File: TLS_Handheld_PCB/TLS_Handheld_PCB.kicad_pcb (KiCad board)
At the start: 4 copper layers, 175 x 100 mm, 89 parts, among them J1 Conn_01x02_Pin, J2 Conn_01x02_Pin, J3 Conn_01x02_Pin, M1 TO-236AB_SOT23_NEX, M2 TO-236AB_SOT23_NEX, U1 LT8640SEV_PBF, U2 LT8640SEV_PBF, U3 LT8619EDD-TRPBF, U4 LAA108STR, U5 SOP65P640X110-14N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

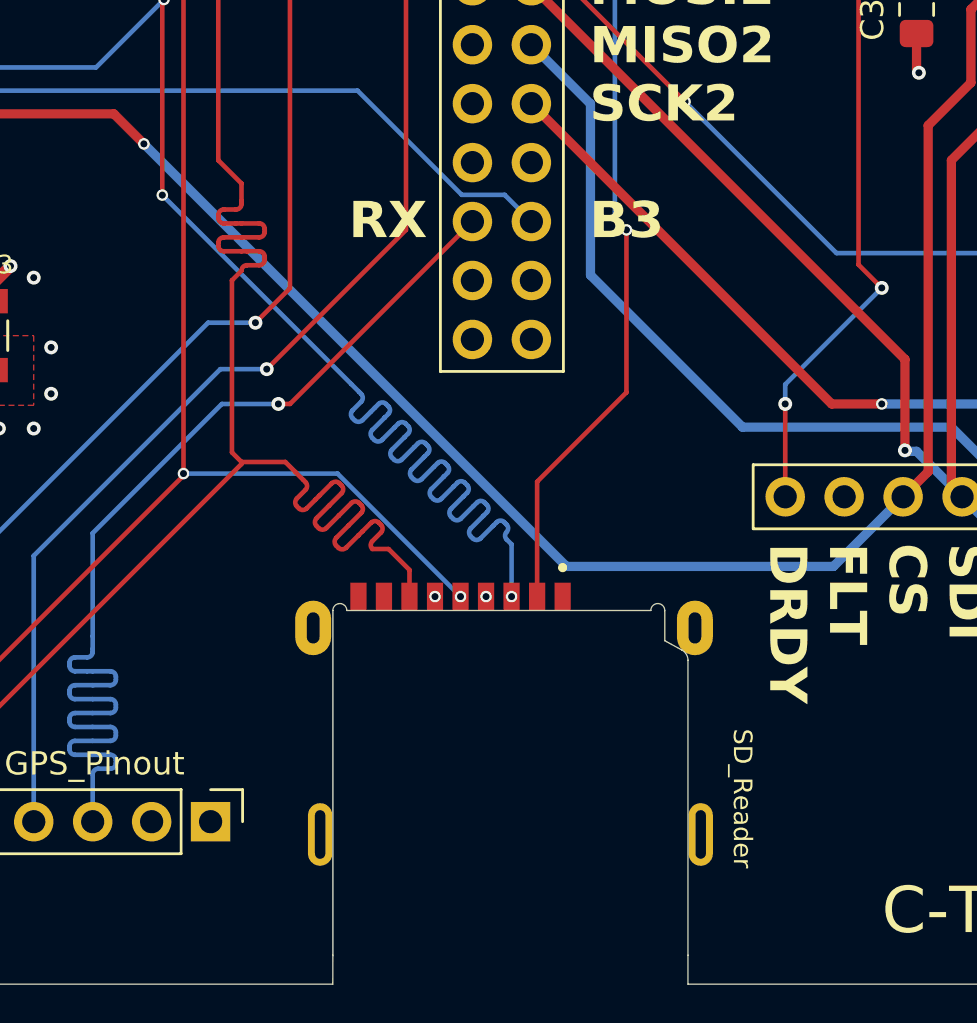
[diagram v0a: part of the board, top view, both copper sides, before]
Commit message: Fix Clearance issues with sd card
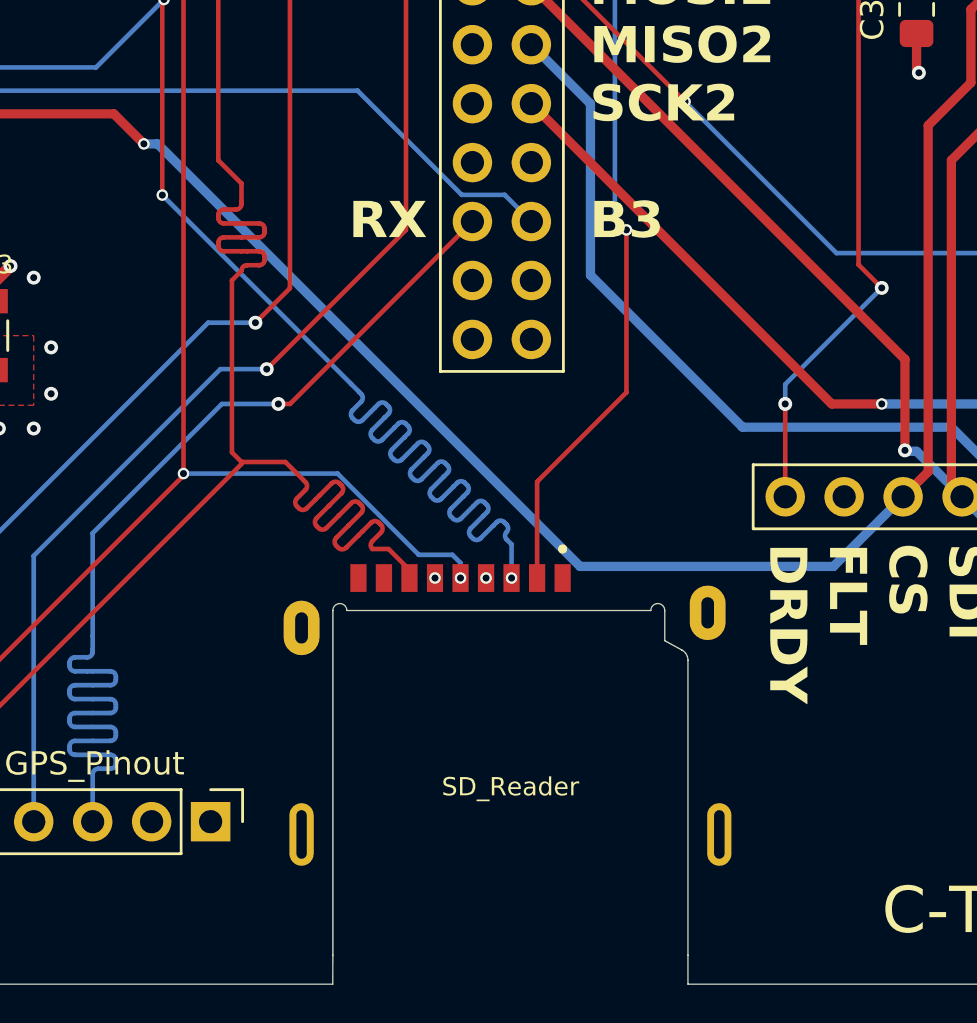
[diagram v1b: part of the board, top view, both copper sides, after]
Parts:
- SD_Reader: footprint My_PCB_Library:CUI_MSD-3-A -> Library:CUI_MSD-3-A
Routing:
- net TOUCH_MISO: track 181.4 -> 180.6 mm
- net DISPL_MOSI: track 211.3 -> 210.5 mm
- net SD_CS: track 60.1 -> 59.3 mm
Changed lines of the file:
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@@
 		(embedded_fonts no)
 	)
-	(footprint "My_PCB_Library:CUI_MSD-3-A"
+	(footprint "Library:CUI_MSD-3-A"
 		(layer "F.Cu")
 		(at 165.5 133.5)
 		(property "Reference" "SD_Reader"
-			(at 10 0.5 270)
-			(unlocked yes)
+			(at 0 0 0)
 			(layer "F.SilkS")
 			(effects
 				(font
-					(size 0.8 0.8)
+					(size 0.787402 0.787402)
 					(thickness 0.15)
 				)
@@
 		(attr smd)
 		(fp_circle
-			(center 2.25 -9.45)
-			(end 2.35 -9.45)
+			(center 2.25 -10.25)
+			(end 2.35 -10.25)
 			(stroke
 				(width 0.2)
@@
 		)
 		(fp_line
-			(start -9.525 -9.05)
-			(end 8.975 -9.05)
+			(start -10.5 -10)
+			(end 9.5 -10)
 			(stroke
 				(width 0.05)
@@
 		)
 		(fp_line
-			(start -9.525 13.1)
-			(end -9.525 -9.05)
+			(start -10.5 13.1)
+			(end -10.5 -10)
 			(stroke
 				(width 0.05)
@@
 		)
 		(fp_line
-			(start 8.975 -9.05)
-			(end 8.975 13.1)
+			(start 9.5 -10)
+			(end 9.5 13.1)
 			(stroke
 				(width 0.05)
@@
 		)
 		(fp_line
-			(start 8.975 13.1)
-			(end -9.525 13.1)
+			(start 9.5 13.1)
+			(end -10.5 13.1)
 			(stroke
 				(width 0.05)
@@
 		)
 		(pad "1" smd rect
-			(at 2.25 -8.2)
+			(at 2.25 -9)
 			(size 0.7 1.2)
 			(layers "F.Cu" "F.Mask" "F.Paste")
@@
 		)
 		(pad "2" smd rect
-			(at 1.15 -8.2)
+			(at 1.15 -9)
 			(size 0.7 1.2)
 			(layers "F.Cu" "F.Mask" "F.Paste")
@@
 		)
 		(pad "3" smd rect
-			(at 0.05 -8.2)
+			(at 0.05 -9)
 			(size 0.7 1.2)
 			(layers "F.Cu" "F.Mask" "F.Paste")
@@
 		)
 		(pad "4" smd rect
-			(at -1.05 -8.2)
+			(at -1.05 -9)
 			(size 0.7 1.2)
 			(layers "F.Cu" "F.Mask" "F.Paste")
@@
 		)
 		(pad "5" smd rect
-			(at -2.15 -8.2)
+			(at -2.15 -9)
 			(size 0.7 1.2)
 			(layers "F.Cu" "F.Mask" "F.Paste")
@@
 		)
 		(pad "6" smd rect
-			(at -3.25 -8.2)
+			(at -3.25 -9)
 			(size 0.7 1.2)
 			(layers "F.Cu" "F.Mask" "F.Paste")
@@
 		)
 		(pad "7" smd rect
-			(at -4.35 -8.2)
+			(at -4.35 -9)
 			(size 0.7 1.2)
 			(layers "F.Cu" "F.Mask" "F.Paste")
@@
 		)
 		(pad "8" smd rect
-			(at -5.45 -8.2)
+			(at -5.45 -9)
 			(size 0.7 1.2)
 			(layers "F.Cu" "F.Mask" "F.Paste")
@@
 		)
 		(pad "CD" smd rect
-			(at -6.55 -8.2)
+			(at -6.55 -9)
 			(size 0.7 1.2)
 			(layers "F.Cu" "F.Mask" "F.Paste")
@@
 		)
 		(pad "G1" thru_hole oval
-			(at -8.5 -6.85)
+			(at -9 -6.85)
 			(size 1.55 2.35)
 			(drill oval 0.55 1.35)
@@
 		)
 		(pad "G2" thru_hole oval
-			(at 7.95 -6.85)
+			(at 8.5 -7.5)
 			(size 1.55 2.35)
 			(drill oval 0.55 1.35)
@@
 		)
 		(pad "G3" thru_hole oval
-			(at -8.2 2.05)
+			(at -9 2.05)
 			(size 1.05 2.7)
 			(drill oval 0.45 2.1)
@@
 		)
 		(pad "G4" thru_hole oval
-			(at 8.2 2.05)
+			(at 9 2.05)
 			(size 1.05 2.7)
 			(drill oval 0.45 2.1)
@@
 		)
 		(embedded_fonts no)
-		(model "C:/Users/cbyer/Documents/_gitRepos/ENGG4000_PowerPCB/Components/SD_Card/MSD_3_A/MSD-3-A.step"
-			(offset
-				(xyz -7.5 -7 -0.85)
-			)
-			(scale
-				(xyz 1 1 1)
-			)
-			(rotate
-				(xyz 90 180 180)
-			)
-		)
 	)
 	(footprint "Capacitor_SMD:C_0805_2012Metric_Pad1.18x1.45mm_HandSolder"
@@
 	)
 	(via
-		(at 162.25 125.3)
+		(at 162.25 124.5)
 		(size 0.5)
 		(drill 0.3)
@@
 	)
 	(segment
-		(start 167.9125 124)
+		(start 168.5 124)
 		(end 179.42 124)
 		(width 0.4)
@@
 	(segment
 		(start 149.70625 105.79375)
-		(end 167.9125 124)
+		(end 150.29375 105.79375)
 		(width 0.4)
 		(layer "B.Cu")
@@
 	)
 	(segment
+		(start 150.29375 105.79375)
+		(end 168.5 124)
+		(width 0.4)
+		(layer "B.Cu")
+		(net 48)
+	)
+	(segment
 		(start 222.065 92.5)
 		(end 221 92.5)
@@
 	)
 	(via
-		(at 164.45 125.3)
+		(at 164.45 124.5)
 		(size 0.5)
 		(drill 0.3)
@@
 	)
 	(via
-		(at 165.55 125.3)
+		(at 165.55 124.5)
 		(size 0.5)
 		(drill 0.3)
@@
 	)
 	(segment
+		(start 165.55 123.05)
+		(end 165.334969 122.834969)
+		(width 0.2)
+		(layer "B.Cu")
+		(net 64)
+	)
+	(segment
 		(start 106.4125 117.5)
 		(end 116.9125 107)
@@
 	)
 	(segment
+		(start 165.55 124.5)
+		(end 165.55 123.05)
+		(width 0.2)
+		(layer "B.Cu")
+		(net 64)
+	)
+	(segment
 		(start 84 109.123531)
 		(end 84 109.243531)
@@
 	)
 	(segment
-		(start 165.55 125.3)
-		(end 165.55 123.05)
-		(width 0.2)
-		(layer "B.Cu")
-		(net 64)
-	)
-	(segment
 		(start 160.933205 118.433204)
 		(end 160.933204 118.433204)
@@
 	)
 	(segment
-		(start 165.55 123.05)
-		(end 165.334969 122.834969)
-		(width 0.2)
-		(layer "B.Cu")
-		(net 64)
-	)
-	(segment
 		(start 147.6425 102.5)
 		(end 150.57125 99.57125)
@@
 	)
 	(via
-		(at 163.35 125.3)
+		(at 163.35 124.5)
 		(size 0.5)
 		(drill 0.3)
@@
 	)
 	(segment
-		(start 151.4125 120)
-		(end 158.05 120)
+		(start 158.7125 81.2)
+		(end 163.8625 81.2)
 		(width 0.2)
 		(layer "B.Cu")
@@
 	)
 	(segment
-		(start 158.7125 81.2)
-		(end 163.8625 81.2)
+		(start 151.4125 89)
+		(end 151.4125 88.5)
 		(width 0.2)
 		(layer "B.Cu")
@@
 	)
 	(segment
-		(start 151.4125 89)
-		(end 151.4125 88.5)
+		(start 151.4125 120)
+		(end 158.05 120)
+		(width 0.2)
+		(layer "B.Cu")
+		(net 65)
+	)
+	(segment
+		(start 158.05 120)
+		(end 161.55 123.5)
 		(width 0.2)
 		(layer "B.Cu")
@@
 	)
 	(segment
-		(start 158.05 120)
-		(end 163.35 125.3)
+		(start 163.35 123.85)
+		(end 163.35 124.5)
+		(width 0.2)
+		(layer "B.Cu")
+		(net 65)
+	)
+	(segment
+		(start 161.55 123.5)
+		(end 163 123.5)
+		(width 0.2)
+		(layer "B.Cu")
+		(net 65)
+	)
+	(segment
+		(start 163 123.5)
+		(end 163.35 123.85)
 		(width 0.2)
 		(layer "B.Cu")
@@
 	)
 	(segment
-		(start 161.15 124.15)
-		(end 160.249758 123.249758)
+		(start 160.249758 123.249758)
+		(end 159.551758 123.249758)
 		(width 0.2)
 		(layer "F.Cu")
@@
 	)
 	(segment
-		(start 161.15 125.3)
+		(start 161.15 124.5)
 		(end 161.15 124.15)
 		(width 0.2)
@@
 	)
 	(segment
-		(start 160.249758 123.249758)
-		(end 159.551758 123.249758)
+		(start 161.15 124.15)
+		(end 160.249758 123.249758)
 		(width 0.2)
 		(layer "F.Cu")
@@
 	(segment
 		(start 166.65 120.35)
-		(end 166.65 125.3)
+		(end 166.65 124.5)
 		(width 0.2)
 		(layer "F.Cu")
@@
 	)
 	(segment
-		(start 170.5 116.5)
-		(end 166.65 120.35)
+		(start 169.5 71.5975)
+		(end 166.4025 68.5)
 		(width 0.2)
 		(layer "F.Cu")
@@
 	)
 	(segment
-		(start 169.5 71.5975)
-		(end 166.4025 68.5)
+		(start 170.5 116.5)
+		(end 166.65 120.35)
 		(width 0.2)
 		(layer "F.Cu")

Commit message: Add marc's changes f=to improve noise of 8 V regulator.
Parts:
- added C: 1uF, CL31B475KBHNFNE:CAPC3216X180N, F.Cu at (130.5, 79.0)
- added C: 1uF, CL31B475KBHNFNE:CAPC3216X180N, F.Cu at (130.5, 111.0)
- C31: value 22uF -> 100uF; footprint KRM55QR71H226KH13K:CAPC6153X390N -> footprints00:CAP_NTJ_76B_9.5T_NIP
- R33: value 120k -> 117k; footprint CRM1206_FX_1203ELF:RESC3116X65N -> RN73R2BTTD1173B50:RESC3216X70N
- moved C31 1.53 mm to (144.5, 55.5)
- moved C17 0.54 mm to (133.5, 112.1)
- moved C27 0.50 mm to (133.5, 80.0)
- moved C29 0.50 mm to (126.0, 82.0)
- moved C19 0.46 mm to (126.0, 114.1)
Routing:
- net GND: track 105.2 -> 114.2 mm, vias 241 -> 238
- net /Pin: track 34.3 -> 32.1 mm, vias 26 -> 23
- net /FB1: track 2.20 -> 3.24 mm
- net /FB2: track 2.14 -> 2.99 mm
- net Net-(U2-INTVCC): track 2.61 -> 3.11 mm

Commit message: Add Marc's minor changes to routing and vias.
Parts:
- moved C18 0.50 mm to (122.0, 124.5)
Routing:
- net GND: track 114.2 -> 115.7 mm, vias 238 -> 204
- net /5V: track 110.7 -> 110.1 mm
